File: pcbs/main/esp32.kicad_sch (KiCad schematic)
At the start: 1 part, among them U1 ESP32-DEVKITC-32U

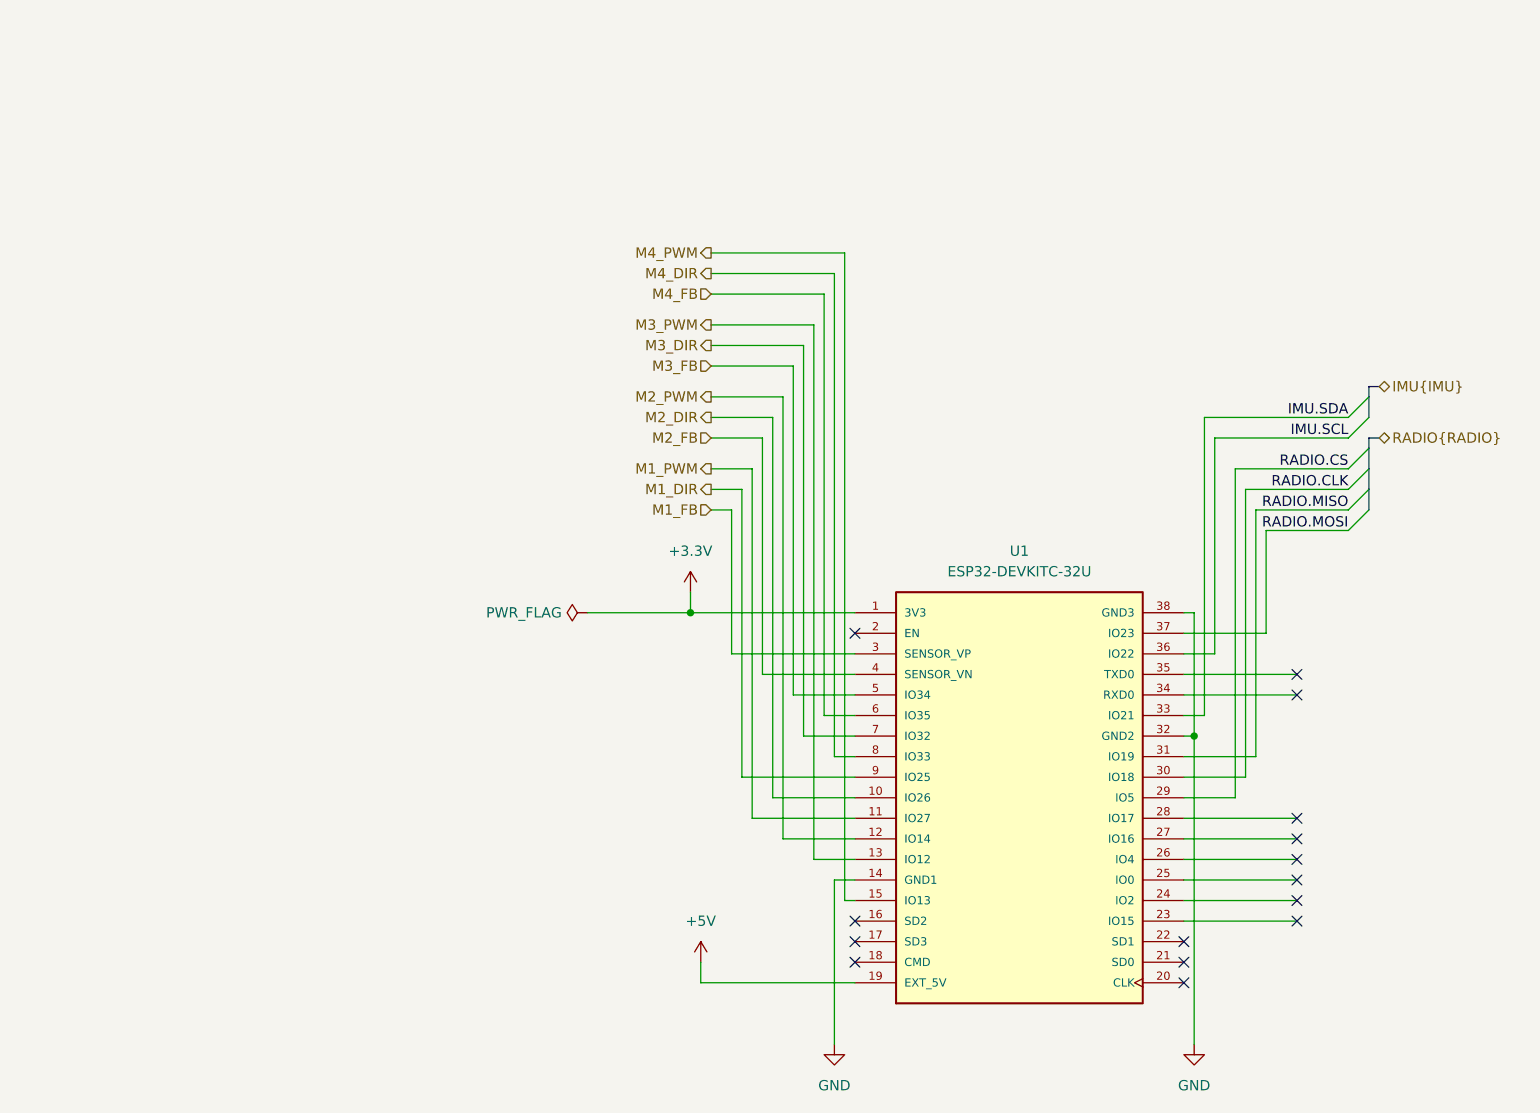
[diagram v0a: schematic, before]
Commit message: First version with 12x8 cm proofboard.
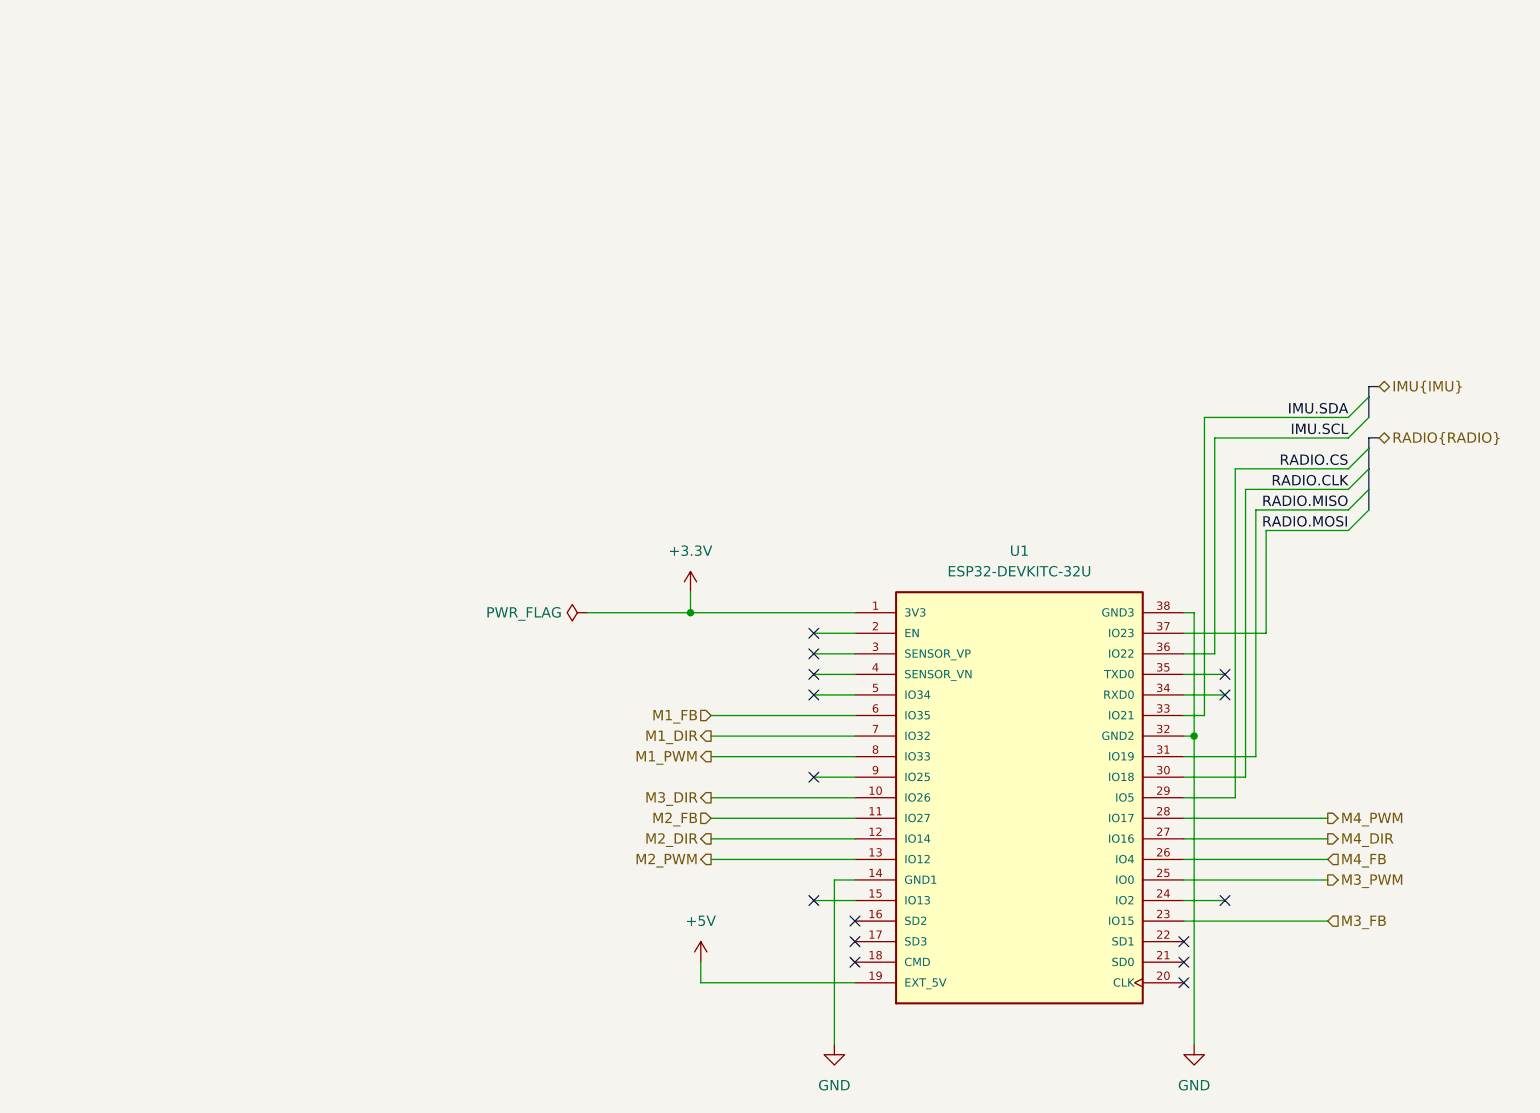
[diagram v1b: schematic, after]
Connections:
- net M1_DIR: now also U1.7 (IO32); no longer U1.9 (IO25)
- net M1_FB: now also U1.6 (IO35); no longer U1.3 (SENSOR_VP)
- net M1_PWM: now also U1.8 (IO33); no longer U1.11 (IO27)
- net M2_DIR: now also U1.12 (IO14); no longer U1.10 (IO26)
- net M2_FB: now also U1.11 (IO27); no longer U1.4 (SENSOR_VN)
- net M2_PWM: now also U1.13 (IO12); no longer U1.12 (IO14)
- net M3_DIR: now also U1.10 (IO26); no longer U1.7 (IO32)
- net M3_FB: now also U1.23 (IO15); no longer U1.5 (IO34)
- net M3_PWM: now also U1.25 (IO0); no longer U1.13 (IO12)
- net M4_DIR: now also U1.27 (IO16); no longer U1.8 (IO33)
- net M4_FB: now also U1.26 (IO4); no longer U1.6 (IO35)
- net M4_PWM: now also U1.28 (IO17); no longer U1.15 (IO13)

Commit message: Edits for custom board
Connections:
- net M4_FB is gone; now on net M3_DIR: U1.26 (IO4)
- net M1_DIR: now also U1.28 (IO17); no longer U1.7 (IO32)
- net M1_PWM: now also U1.7 (IO32); no longer U1.8 (IO33)
- net M2_DIR: now also U1.27 (IO16); no longer U1.12 (IO14)
- net M2_PWM: now also U1.8 (IO33); no longer U1.13 (IO12)
- net M3_DIR: no longer U1.10 (IO26)
- net M3_PWM: now also U1.9 (IO25); no longer U1.25 (IO0)
- net M4_DIR: now also U1.25 (IO0); no longer U1.27 (IO16)
- net M4_PWM: now also U1.10 (IO26); no longer U1.28 (IO17)
- net Blink_IO: now reaches U1.24 (IO2)
- net M1_ENC: now reaches U1.3 (SENSOR_VP)
- net KICKER_EN: now reaches U1.34 (RXD0)
- net KICKER_PWM: now reaches U1.35 (TXD0)
- net M2_ENC: now reaches U1.4 (SENSOR_VN)
- net M3_ENC: now reaches U1.5 (IO34)
- net M1_FB renamed M4_ENC
- net M2_FB: no longer names the net of U1.11 (IO27)
- net M3_FB renamed RADIO.CE
- no-connect marks 15 -> 7
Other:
- moved on the sheet: U1

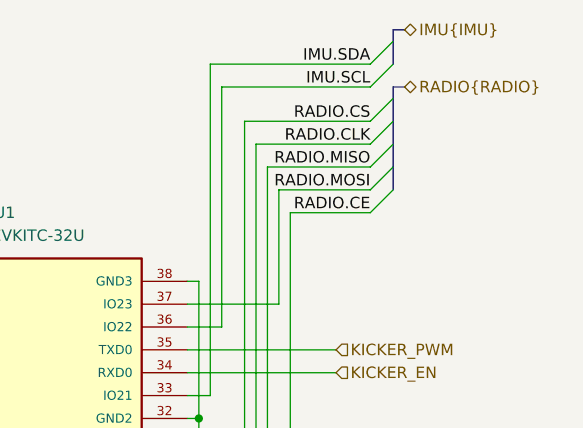
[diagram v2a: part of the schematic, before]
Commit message: feat: radio and motor encoders
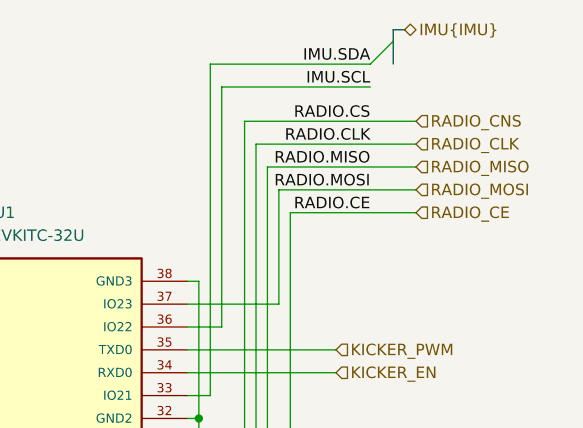
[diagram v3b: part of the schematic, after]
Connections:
- net RADIO.CE renamed RADIO_CE
- net RADIO.CLK renamed RADIO_CLK
- net RADIO.CS renamed RADIO_CNS
- net RADIO.MISO renamed RADIO_MISO
- net RADIO.MOSI renamed RADIO_MOSI

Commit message: feat: imu
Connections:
- net IMU.SCL renamed IMU_SCL
- net IMU.SDA renamed IMU_SDA
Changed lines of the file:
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@@
 		(at 115.57 93.98)
 	)
-	(bus_entry
-		(at 138.43 21.59)
-		(size -2.54 2.54)
-		(stroke
-			(width 0)
-			(type default)
-		)
-	)
 	(wire
 		(pts
@@
 		)
 	)
-	(bus
-		(pts
-			(xy 138.43 20.32) (xy 138.43 21.59)
-		)
-		(stroke
-			(width 0)
-			(type default)
-		)
-	)
 	(wire
 		(pts
@@
 	(wire
 		(pts
-			(xy 135.89 26.67) (xy 119.38 26.67)
+			(xy 119.38 26.67) (xy 140.97 26.67)
 		)
 		(stroke
@@
 		)
 	)
-	(bus
-		(pts
-			(xy 138.43 21.59) (xy 138.43 24.13)
-		)
-		(stroke
-			(width 0)
-			(type default)
-		)
-	)
 	(wire
 		(pts
@@
 	(wire
 		(pts
-			(xy 135.89 24.13) (xy 118.11 24.13)
+			(xy 118.11 24.13) (xy 140.97 24.13)
 		)
 		(stroke
@@
 		(pts
 			(xy 57.15 63.5) (xy 74.93 63.5)
-		)
-		(stroke
-			(width 0)
-			(type default)
-		)
-	)
-	(bus
-		(pts
-			(xy 139.7 20.32) (xy 138.43 20.32)
 		)
 		(stroke
@@
 		)
 	)
+	(hierarchical_label "IMU_SCL"
+		(shape input)
+		(at 140.97 26.67 0)
+		(effects
+			(font
+				(size 1.27 1.27)
+			)
+			(justify left)
+		)
+	)
 	(hierarchical_label "M4_PWM"
 		(shape output)
@@
 		)
 	)
+	(hierarchical_label "IMU_SDA"
+		(shape input)
+		(at 140.97 24.13 0)
+		(effects
+			(font
+				(size 1.27 1.27)
+			)
+			(justify left)
+		)
+	)
 	(hierarchical_label "M1_PWM"
 		(shape output)
@@
 		)
 	)
-	(hierarchical_label "IMU{IMU}"
-		(shape bidirectional)
-		(at 139.7 20.32 0)
-		(effects
-			(font
-				(size 1.27 1.27)
-			)
-			(justify left)
-		)
-	)

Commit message: fea: add jumpers to I2C encoders config
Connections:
- net IMU_SCL renamed SCL
- net IMU_SDA renamed SDA
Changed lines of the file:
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@@
 		)
 	)
-	(hierarchical_label "IMU_SCL"
-		(shape input)
+	(hierarchical_label "SCL"
+		(shape bidirectional)
 		(at 140.97 26.67 0)
 		(effects
@@
 		)
 	)
-	(hierarchical_label "IMU_SDA"
-		(shape input)
+	(hierarchical_label "SDA"
+		(shape bidirectional)
 		(at 140.97 24.13 0)
 		(effects
